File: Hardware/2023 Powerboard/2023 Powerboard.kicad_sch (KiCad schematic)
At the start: 153 parts, among them J1 RJ45_LED_Shielded, J2 6P6C, Q1 BSS138, Q10 BSS138, Q11 QM6015D, Q12 IRF7606PBF, Q13 BSS138, Q14 QM6015D, Q15 BSS138, Q16 IRF7606PBF, Q17 BSS138, Q18 QM6015D, Q19 BSS138, Q2 BSS138, Q20 BSS138, Q21 IRF7606PBF, Q22 QM6015D, Q23 BSS138, Q24 BSS138, Q25 IRF7606PBF, Q26 QM6015D, Q27 BSS138, Q28 BSS138, Q29 IRF7606PBF, Q3 QM6015D, Q30 QM6015D, Q31 BSS138, Q32 QM6015D, Q4 IRF7606PBF, Q5 BSS138, Q6 BSS138, Q7 QM6015D, Q8 IRF7606PBF, Q9 BSS138, U1 3V3, U2 Teensy4.1_DEV-16771

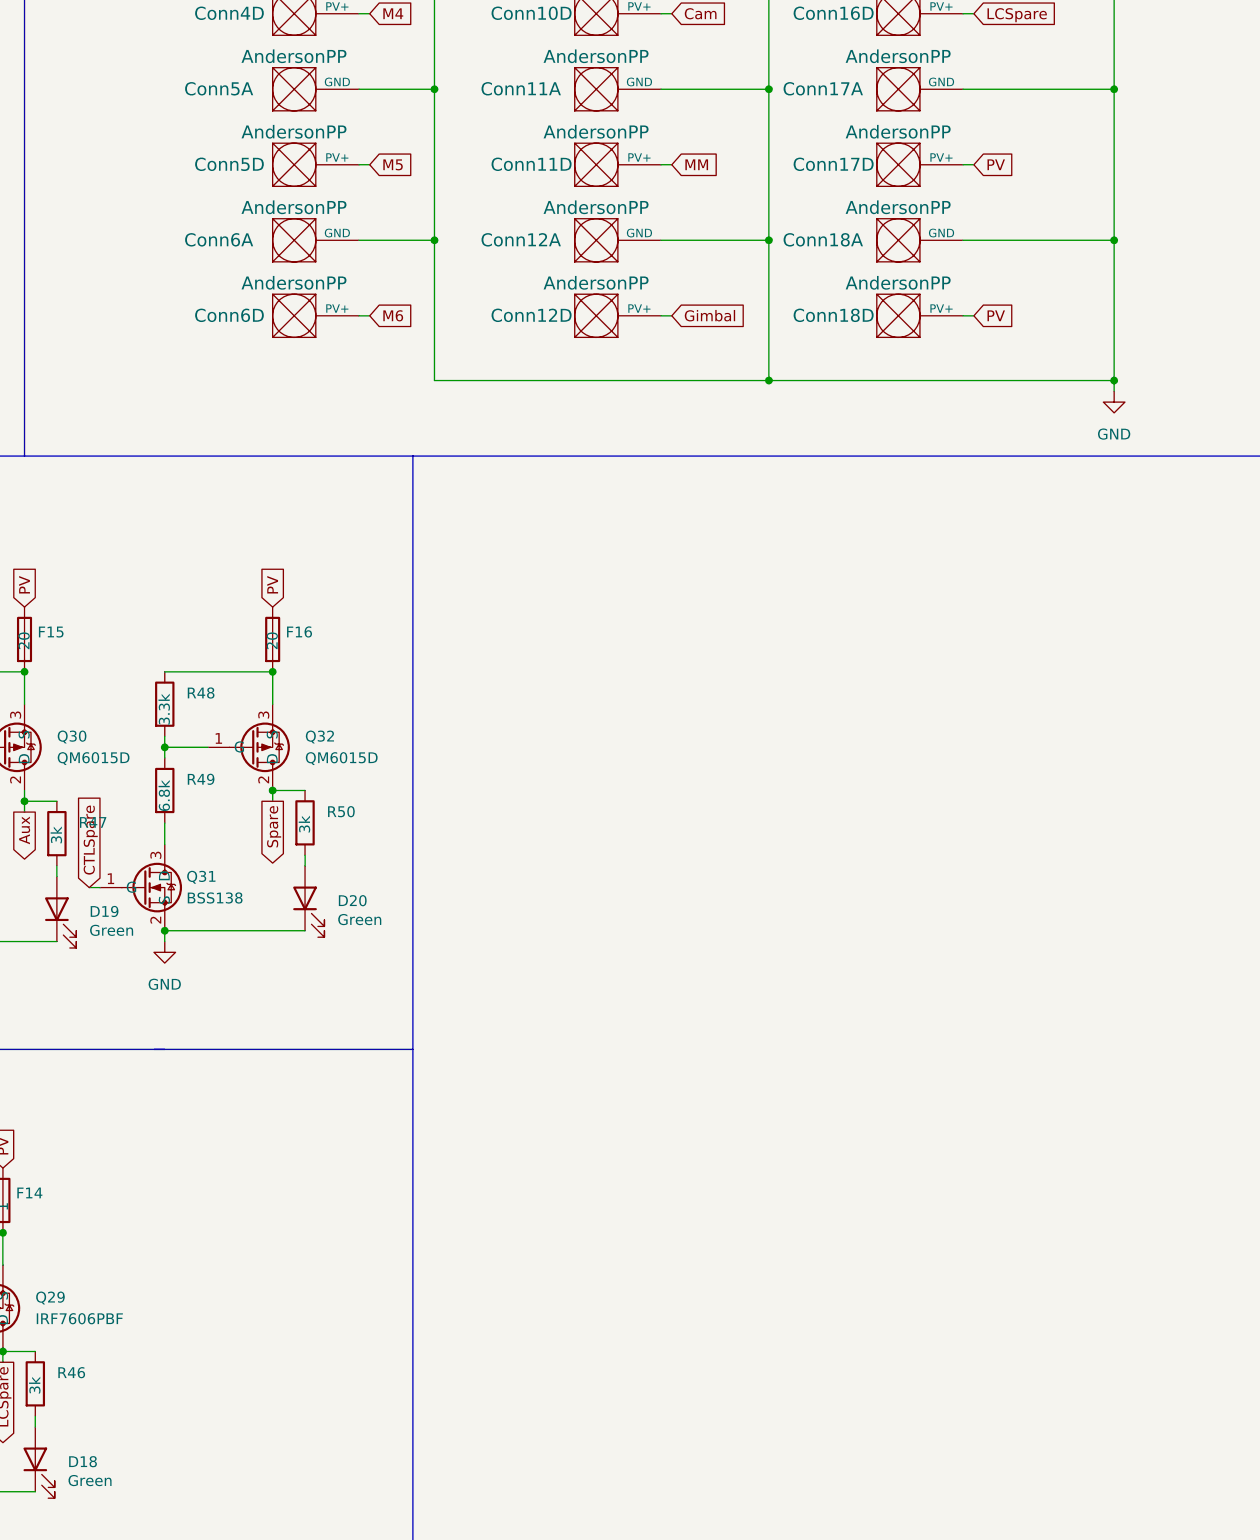
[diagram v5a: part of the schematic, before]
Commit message: Added Fuses, Potential Layout for Connector 1
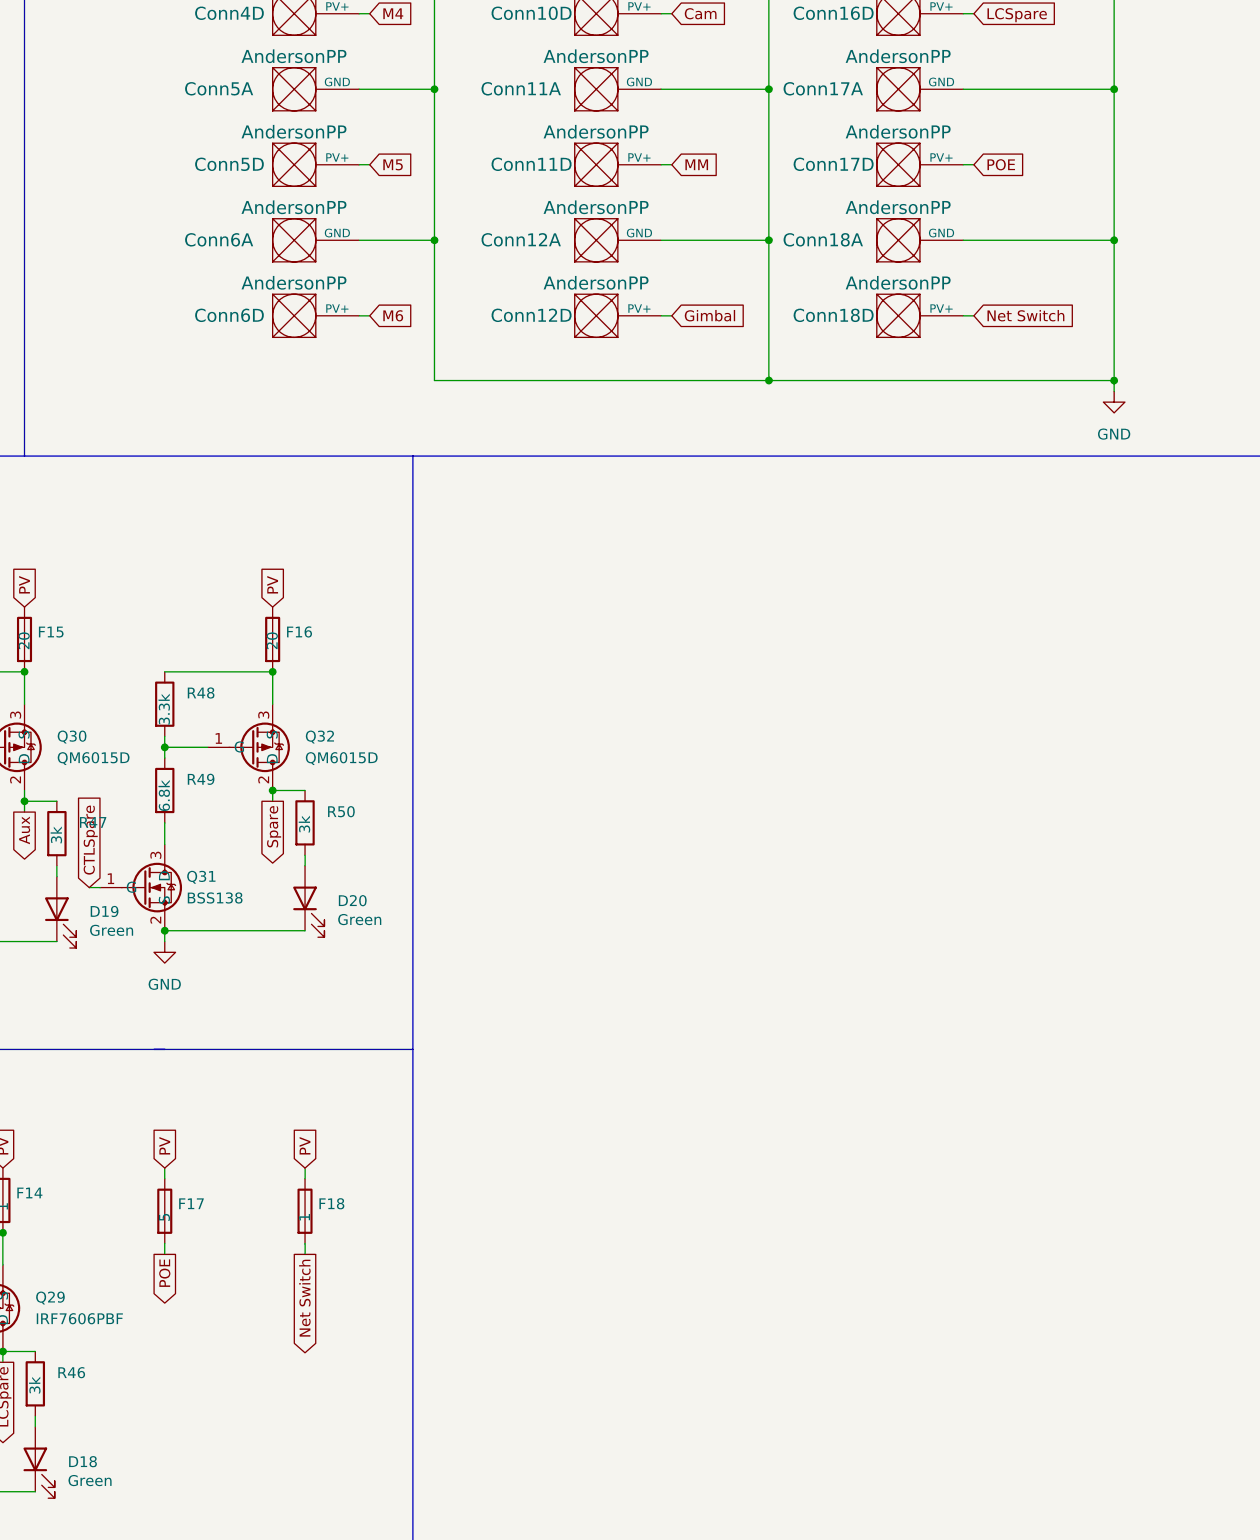
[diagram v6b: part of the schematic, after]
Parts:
- added F17: 5, MRDT_Passives:ATC_Fuse_Block, symbol Device:Fuse
- added F18: 1, MRDT_Passives:ATC_Fuse_Block, symbol Device:Fuse
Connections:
- net PV: now also F17.1, F18.1; no longer Conn17.4 (PV+), Conn18.4 (PV+)
- new net Net Switch: Conn18.4 (PV+), F18.2
- new net POE: Conn17.4 (PV+), F17.2
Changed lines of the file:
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@@
     (stroke (width 0) (type default) (color 0 0 0 0))
   )
+  (wire (pts (xy 281.94 238.76) (xy 281.94 240.03))
+    (stroke (width 0) (type default) (color 0 0 0 0))
+  )
   (wire (pts (xy 100.33 245.11) (xy 100.33 246.38))
     (stroke (width 0) (type default) (color 0 0 0 0))
@@
     (stroke (width 0) (type default) (color 0 0 0 0))
   )
+  (wire (pts (xy 265.43 229.87) (xy 265.43 231.14))
+    (stroke (width 0) (type default) (color 0 0 0 0))
+  )
   (wire (pts (xy 66.04 255.27) (xy 66.04 257.81))
     (stroke (width 0) (type default) (color 0 0 0 0))
@@
     (stroke (width 0) (type default) (color 0 0 0 0))
   )
+  (wire (pts (xy 281.94 229.87) (xy 281.94 231.14))
+    (stroke (width 0) (type default) (color 0 0 0 0))
+  )
   (wire (pts (xy 20.32 31.75) (xy 20.32 34.29))
     (stroke (width 0) (type default) (color 0 0 0 0))
@@
     (stroke (width 0) (type default) (color 0 0 0 0))
   )
+  (wire (pts (xy 265.43 238.76) (xy 265.43 240.03))
+    (stroke (width 0) (type default) (color 0 0 0 0))
+  )
   (wire (pts (xy 22.86 43.18) (xy 31.75 43.18))
     (stroke (width 0) (type default) (color 0 0 0 0))
@@
     )
   )
-  (global_label "PV" (shape input) (at 360.68 129.54 0) (fields_autoplaced)
+  (global_label "Net Switch" (shape input) (at 360.68 129.54 0) (fields_autoplaced)
     (effects (font (size 1.27 1.27)) (justify left))
-    (property "Intersheet References" "${INTERSHEET_REFS}" (id 0) (at 365.4517 129.4606 0)
+    (property "Intersheet References" "${INTERSHEET_REFS}" (id 0) (at 373.3136 129.4606 0)
       (effects (font (size 1.27 1.27)) (justify left) hide)
     )
@@
     )
   )
+  (global_label "PV" (shape input) (at 265.43 229.87 90) (fields_autoplaced)
+    (effects (font (size 1.27 1.27)) (justify left))
+    (property "Intersheet References" "${INTERSHEET_REFS}" (id 0) (at 265.3506 225.0983 90)
+      (effects (font (size 1.27 1.27)) (justify left) hide)
+    )
+  )
   (global_label "CTLLCSpare" (shape input) (at 224.79 262.89 90) (fields_autoplaced)
     (effects (font (size 1.27 1.27)) (justify left))
@@
     )
   )
+  (global_label "POE" (shape output) (at 265.43 240.03 270) (fields_autoplaced)
+    (effects (font (size 1.27 1.27)) (justify right))
+    (property "Intersheet References" "${INTERSHEET_REFS}" (id 0) (at 265.3506 246.1926 90)
+      (effects (font (size 1.27 1.27)) (justify right) hide)
+    )
+  )
+  (global_label "Net Switch" (shape output) (at 281.94 240.03 270) (fields_autoplaced)
+    (effects (font (size 1.27 1.27)) (justify right))
+    (property "Intersheet References" "${INTERSHEET_REFS}" (id 0) (at 281.8606 252.6636 90)
+      (effects (font (size 1.27 1.27)) (justify right) hide)
+    )
+  )
   (global_label "PV" (shape input) (at 73.66 163.83 90) (fields_autoplaced)
     (effects (font (size 1.27 1.27)) (justify left))
@@
     )
   )
+  (global_label "PV" (shape input) (at 281.94 229.87 90) (fields_autoplaced)
+    (effects (font (size 1.27 1.27)) (justify left))
+    (property "Intersheet References" "${INTERSHEET_REFS}" (id 0) (at 281.8606 225.0983 90)
+      (effects (font (size 1.27 1.27)) (justify left) hide)
+    )
+  )
   (global_label "Drive" (shape output) (at 147.32 252.73 270) (fields_autoplaced)
     (effects (font (size 1.27 1.27)) (justify right))
@@
     )
   )
-  (global_label "PV" (shape input) (at 360.68 111.76 0) (fields_autoplaced)
+  (global_label "POE" (shape input) (at 360.68 111.76 0) (fields_autoplaced)
     (effects (font (size 1.27 1.27)) (justify left))
-    (property "Intersheet References" "${INTERSHEET_REFS}" (id 0) (at 365.4517 111.6806 0)
+    (property "Intersheet References" "${INTERSHEET_REFS}" (id 0) (at 366.8426 111.6806 0)
       (effects (font (size 1.27 1.27)) (justify left) hide)
     )
@@
     (pin "2")
   )
+  (symbol (lib_id "Device:Fuse") (at 265.43 234.95 0) (unit 1)
+    (in_bom yes) (on_board yes)
+    (property "Reference" "F17" (id 0) (at 266.954 234.1153 0)
+      (effects (font (size 1.27 1.27)) (justify left))
+    )
+    (property "Value" "5" (id 1) (at 265.43 236.22 90)
+      (effects (font (size 1.27 1.27)) (justify left))
+    )
+    (property "Footprint" "MRDT_Passives:ATC_Fuse_Block" (id 2) (at 263.652 234.95 90)
+      (effects (font (size 1.27 1.27)) hide)
+    )
+    (property "Datasheet" "~" (id 3) (at 265.43 234.95 0)
+      (effects (font (size 1.27 1.27)) hide)
+    )
+    (pin "1")
+    (pin "2")
+  )
   (symbol (lib_id "power:GND") (at 66.04 269.24 0) (unit 1)
     (in_bom yes) (on_board yes) (fields_autoplaced)
@@
     (pin "3")
   )
+  (symbol (lib_id "Device:Fuse") (at 281.94 234.95 0) (unit 1)
+    (in_bom yes) (on_board yes)
+    (property "Reference" "F18" (id 0) (at 283.464 234.1153 0)
+      (effects (font (size 1.27 1.27)) (justify left))
+    )
+    (property "Value" "1" (id 1) (at 281.94 236.22 90)
+      (effects (font (size 1.27 1.27)) (justify left))
+    )
+    (property "Footprint" "MRDT_Passives:ATC_Fuse_Block" (id 2) (at 280.162 234.95 90)
+      (effects (font (size 1.27 1.27)) hide)
+    )
+    (property "Datasheet" "~" (id 3) (at 281.94 234.95 0)
+      (effects (font (size 1.27 1.27)) hide)
+    )
+    (pin "1")
+    (pin "2")
+  )
   (symbol (lib_id "Device:R") (at 100.33 241.3 0) (unit 1)
     (in_bom yes) (on_board yes)
@@
       (reference "F16") (unit 1) (value "20") (footprint "MRDT_Passives:ATC_Fuse_Block")
     )
+    (path "/19d98309-ed6c-4dd8-9d53-20cfb8e347da"
+      (reference "F17") (unit 1) (value "5") (footprint "MRDT_Passives:ATC_Fuse_Block")
+    )
+    (path "/dd62605c-6d8c-40af-b685-0d3331711451"
+      (reference "F18") (unit 1) (value "1") (footprint "MRDT_Passives:ATC_Fuse_Block")
+    )
     (path "/cec99afc-23ee-4368-b3e0-ed620092ff72"

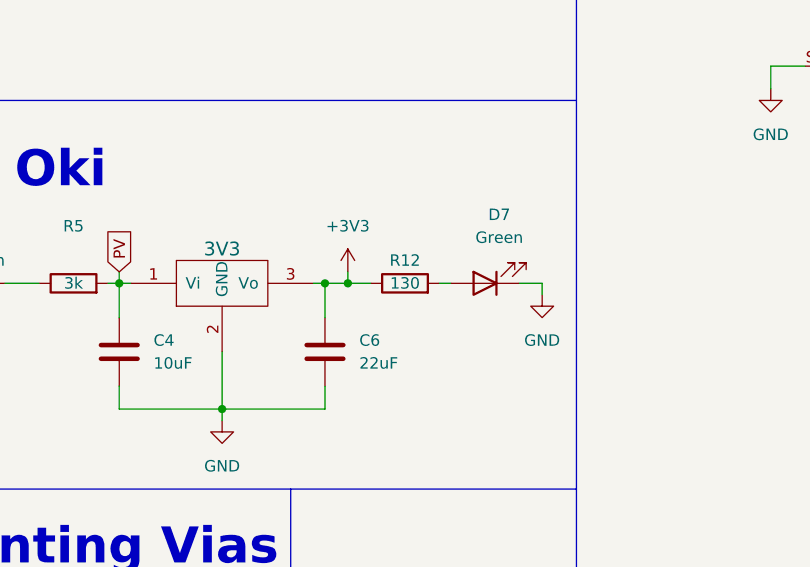
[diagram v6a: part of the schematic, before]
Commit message: Changed resistor value
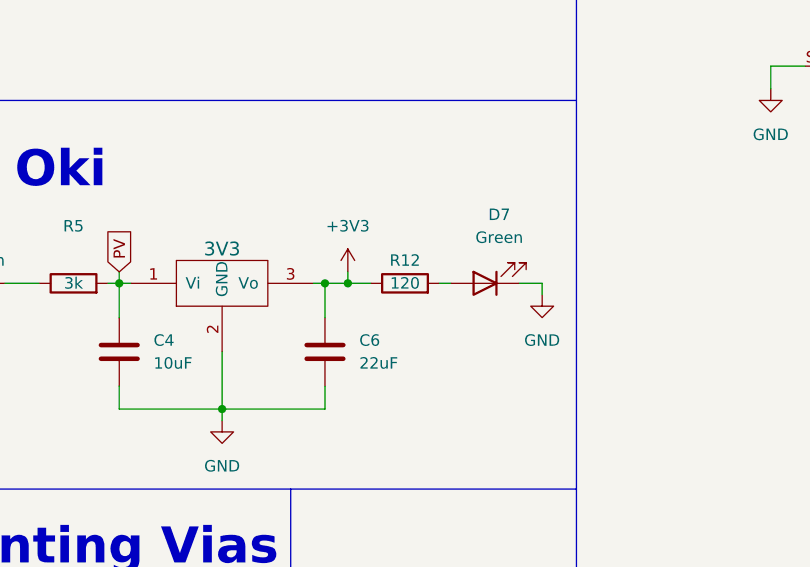
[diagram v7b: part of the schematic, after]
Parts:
- R12: value 130 -> 120
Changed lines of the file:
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@@
     (in_bom yes) (on_board yes)
     (property "Reference" "R12" (id 0) (at 72.39 82.55 90))
-    (property "Value" "130" (id 1) (at 72.39 85.09 90))
+    (property "Value" "120" (id 1) (at 72.39 85.09 90))
     (property "Footprint" "Resistor_SMD:R_0603_1608Metric_Pad0.98x0.95mm_HandSolder" (id 2) (at 72.39 86.868 90)
       (effects (font (size 1.27 1.27)) hide)
@@
     )
     (path "/34a585e0-67c3-431f-9e47-cee333acf604"
-      (reference "R12") (unit 1) (value "130") (footprint "Resistor_SMD:R_0603_1608Metric_Pad0.98x0.95mm_HandSolder")
+      (reference "R12") (unit 1) (value "120") (footprint "Resistor_SMD:R_0603_1608Metric_Pad0.98x0.95mm_HandSolder")
     )
     (path "/4876b0fa-0529-4d71-ad64-ca036afc489c"

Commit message: Layout Review Changes
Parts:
- added D21, D22: Green, LED_SMD:LED_0603_1608Metric_Pad1.05x0.95mm_HandSolder, symbol Device:LED
- added R51, R52: 3k, Resistor_SMD:R_0603_1608Metric_Pad0.98x0.95mm_HandSolder, symbol Device:R
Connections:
- net CTLBB: now also U2.25 (A11); no longer U2.14 (A0)
- net CTLLCSpare: now also U2.24 (A10); no longer U2.15 (A1)
- net CTLNav: now also U2.26 (A12); no longer U2.13 (SCK)
- net GND: now also D21.1 (K), D22.1 (K)
- net Net Switch: now also R52.1
- net POE: now also R51.1
- new net: D21.2 (A), R51.2
- new net: D22.2 (A), R52.2
- no-connect marks 42 -> 41
